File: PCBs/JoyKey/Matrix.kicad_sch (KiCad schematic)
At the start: 19 parts, among them J5 Top Trigger 1, J6 Top Trigger 2, SW2 SW_Push_45deg, SW3 SW_Push_45deg, SW4 SW_Push_45deg, SW5 SW_Push_45deg, SW6 SW_Push_45deg, SW7 SW_Push_45deg

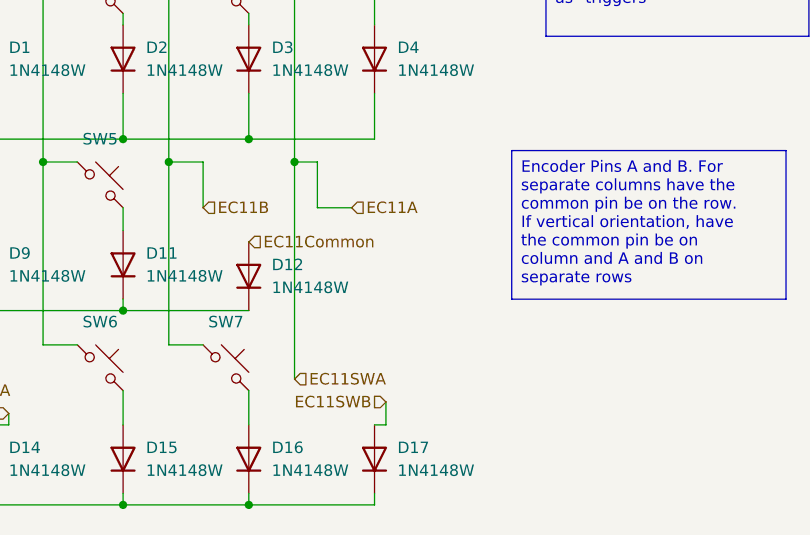
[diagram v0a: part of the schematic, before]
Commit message: Switched encoder to Alps EC12
I wanted something shorter and that didn't have a metal screw post. I do loose out on the switch though, which I've exposed via a separate header
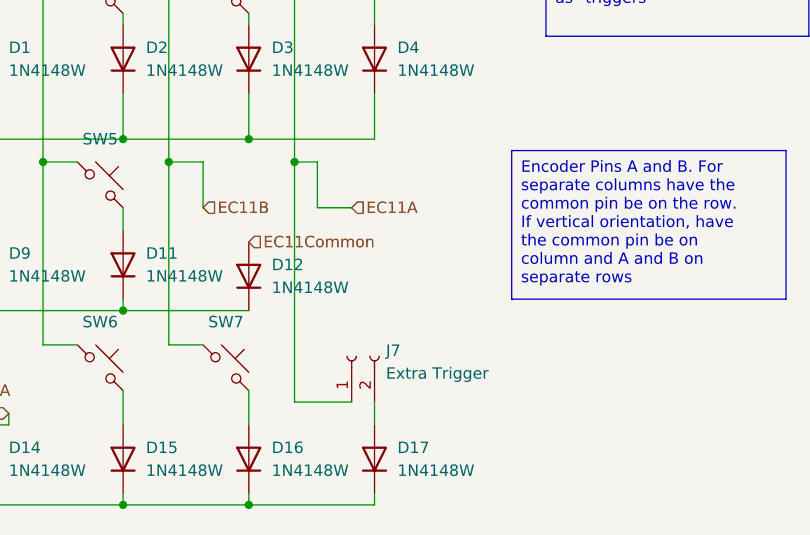
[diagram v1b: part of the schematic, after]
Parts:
- added J7: Extra Trigger, Connector_PinHeader_2.54mm:PinHeader_1x02_P2.54mm_Vertical, symbol Connector:Conn_01x02_Socket
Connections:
- net COL3: now also J7.1 (Pin_1)
- net EC11SWB: no longer names the net of D17.2 (A)
- net EC11SWB: now also J7.2 (Pin_2)
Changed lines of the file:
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@@
 	(wire
 		(pts
-			(xy 165.1 115.57) (xy 165.1 113.03)
-		)
-		(stroke
-			(width 0)
-			(type default)
-		)
-	)
-	(wire
-		(pts
-			(xy 163.83 115.57) (xy 165.1 115.57)
+			(xy 163.83 115.57) (xy 163.83 113.03)
 		)
 		(stroke
@@
 	(wire
 		(pts
+			(xy 154.94 86.36) (xy 154.94 113.03)
+		)
+		(stroke
+			(width 0)
+			(type default)
+		)
+	)
+	(wire
+		(pts
 			(xy 161.29 91.44) (xy 157.48 91.44)
 		)
@@
 	(wire
 		(pts
-			(xy 154.94 86.36) (xy 154.94 110.49)
-		)
-		(stroke
-			(width 0)
-			(type default)
-		)
-	)
-	(wire
-		(pts
 			(xy 149.86 83.82) (xy 163.83 83.82)
 		)
@@
 		(pts
 			(xy 163.83 123.19) (xy 163.83 124.46)
+		)
+		(stroke
+			(width 0)
+			(type default)
+		)
+	)
+	(wire
+		(pts
+			(xy 154.94 113.03) (xy 161.29 113.03)
 		)
 		(stroke
@@
 		)
 	)
-	(hierarchical_label "EC11SWB"
-		(shape input)
-		(at 165.1 113.03 180)
-		(effects
-			(font
-				(size 1.27 1.27)
-			)
-			(justify right)
-		)
-	)
 	(hierarchical_label "StickButtonA"
 		(shape input)
@@
 			)
 			(justify right)
-		)
-	)
-	(hierarchical_label "EC11SWA"
-		(shape input)
-		(at 154.94 110.49 0)
-		(effects
-			(font
-				(size 1.27 1.27)
-			)
-			(justify left)
 		)
 	)
@@
 					(unit 1)
 				)
+			)
+		)
+	)
+	(symbol
+		(lib_id "Connector:Conn_01x02_Socket")
+		(at 161.29 107.95 90)
+		(unit 1)
+		(exclude_from_sim no)
+		(in_bom yes)
+		(on_board yes)
+		(dnp no)
+		(fields_autoplaced yes)
+		(property "Reference" "J7"
+			(at 165.1 107.3149 90)
+			(effects
+				(font
+					(size 1.27 1.27)
+				)
+				(justify right)
+			)
+		)
+		(property "Value" "Extra Trigger"
+			(at 165.1 109.8549 90)
+			(effects
+				(font
+					(size 1.27 1.27)
+				)
+				(justify right)
+			)
+		)
+		(property "Footprint" "Connector_PinHeader_2.54mm:PinHeader_1x02_P2.54mm_Vertical"
+			(at 161.29 107.95 0)
+			(effects
+				(font
+					(size 1.27 1.27)
+				)
+				(hide yes)
+			)
+		)
+		(property "Datasheet" "~"
+			(at 161.29 107.95 0)
+			(effects
+				(font
+					(size 1.27 1.27)
+				)
+				(hide yes)
+			)
+		)
+		(property "Description" "Generic connector, single row, 01x02, script generated"
+			(at 161.29 107.95 0)
+			(effects
+				(font
+					(size 1.27 1.27)
+				)
+				(hide yes)
+			)
+		)
+		(pin "2"
+		)
+		(pin "1"
+		)
+		(instances
+			(project "JoyKey"
+				(path "/7995ec7a-c14b-437e-b354-3eb74052b7cb/68ef131f-9d28-47fd-9e2d-054e6cdf50c5"
+					(reference "J7")
+					(unit 1)
+				)
